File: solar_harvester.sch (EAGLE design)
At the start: 49 parts, among them U1 BQ25505, U2 TPS61322XA, U3 TPS61322XA, U4 MAX17040, U5 INA226

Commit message: schematic complete v01. Caps and diode selection needed
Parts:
- added B1: SOLAR_HARVESTER_M1_BOARD, vrlib_board:SOLAR_HARVESTER_M1_BOARD
- added C10, C9: 22u, vrlib_caps:1608_CAP
- added JP1: (no value), pinhead:PINHD-1X3
- added S1, S2: CONN_SCEW_TYPE_2P, vrlib_connector:CONN_SCEW_TYPE_2P
- added U$23, U$24, U$25, U$26, U$27: LOUT, vrlib_com_symbols:LOUT
- added U$28: GND, vrlib_com_symbols:GND
- C1: value 0.01uF -> 0.01u
- C2: value 4u7F -> 4u7
- C3: value 100uF -> 100u
- C4: value 4u7F -> 10u
- C5, C8: value 0.1uF -> 0.1u
- C6: value 1uF -> 1u
- C7: value 10nF -> 10n
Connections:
- new net GND1: C6.2, C7.2, C8.2, U4.CTG, U4.EO, U4.EP, U4.GND, U4.SEO, U5.A0, U5.A1, U5.GND
- net GND: now also C10.1, C9.1, S1.GND, S2.GND; no longer C6.2, C7.2, C8.2, U4.CTG, U4.EO, U4.EP, U4.GND, U4.SEO, U5.A0, U5.A1, U5.GND
- net I2C_SCL: now also JP1.3
- net I2C_SDA: now also JP1.2
- net VBAT_OK: now also JP1.1
- net VCC: no longer C4.1, C5.1
- net VDD3V3: now also C9.2, S1.VIN
- net VDD5: now also C10.2, S2.VIN
- net VIN_BAT: now also C4.1, C5.1, L2.1, L3.1
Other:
- note added: "I2C & BAT_OK PINHEAD"
- note added: "I2C ADDRESS 0110110"
- note added: "POWER"
- note added: "POWER BOOST"
- note added: "POWER HARVESTING"
- note added: "POWER MEASUREMENT"
- note added: "POWER OUTPUT"
- note added: "Universidad Jaime I. HPCA (High Performance Computer Architecture) Research Group"
- note added: "Vladislav Rykov"
- note added: "solar_harvester_m1"

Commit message: board routing started
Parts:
- removed BAT, SOLAR: CONN_SCEW_TYPE_2P, vrlib_connector:CONN_SCEW_TYPE_2P
- added BAT_IN, PV_IN: CONN_SCEW_TYPE_2P, vrlib_connector:CONN_SCEW_TYPE_2P
- added C11: 4u7, vrlib_caps:0603_CERAMIC
- added D1: JDH2S02SL, vrlib_diode:JDH2S02SL
- renumbered S1 to 3V3_OUT, S2 to 5V_OUT
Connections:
- removed net VCC: C8.1, U1.VOC_SAMP, U1.VSTOR, U5.VS
- new net N$9: D1.P$2, PV_IN.VIN
- new net VSTOR: C11.1, C5.1, C8.1, U1.VOC_SAMP, U1.VSTOR, U5.VS
- net GND: now also BAT_IN.GND, C11.2, PV_IN.GND; no longer BAT.GND, SOLAR.GND
- net PVIN: now also D1.P$1; no longer SOLAR.VIN
- net VIN_BAT: now also BAT_IN.VIN; no longer BAT.VIN, C5.1
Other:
- moved on the sheet: C4, C5

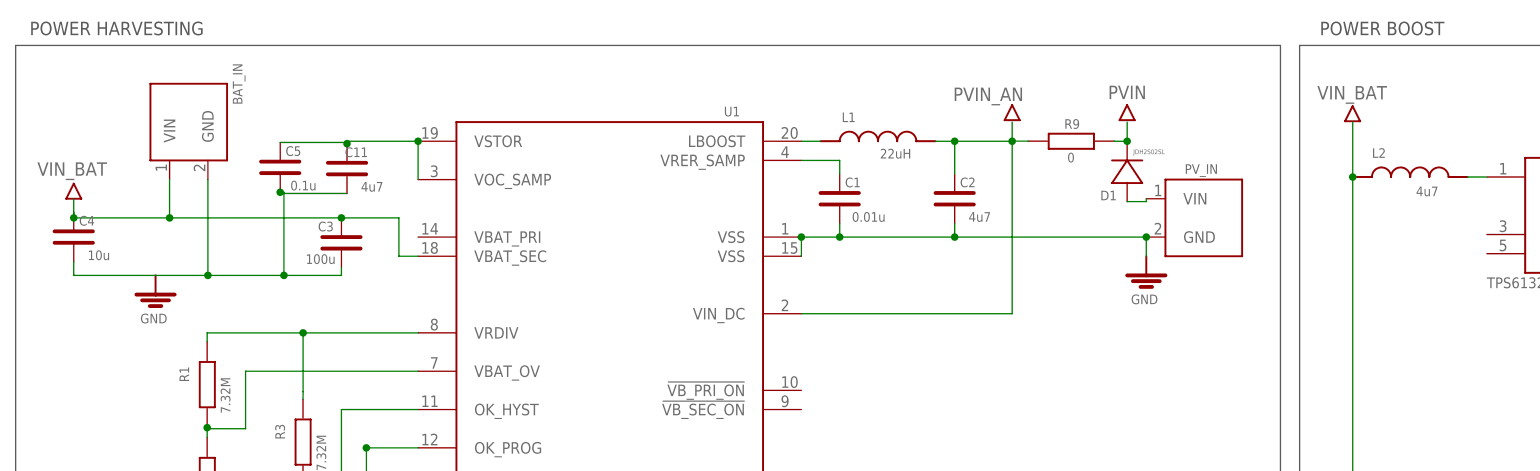
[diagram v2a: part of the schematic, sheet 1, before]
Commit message: bq25505, both tps622, max17004 routed
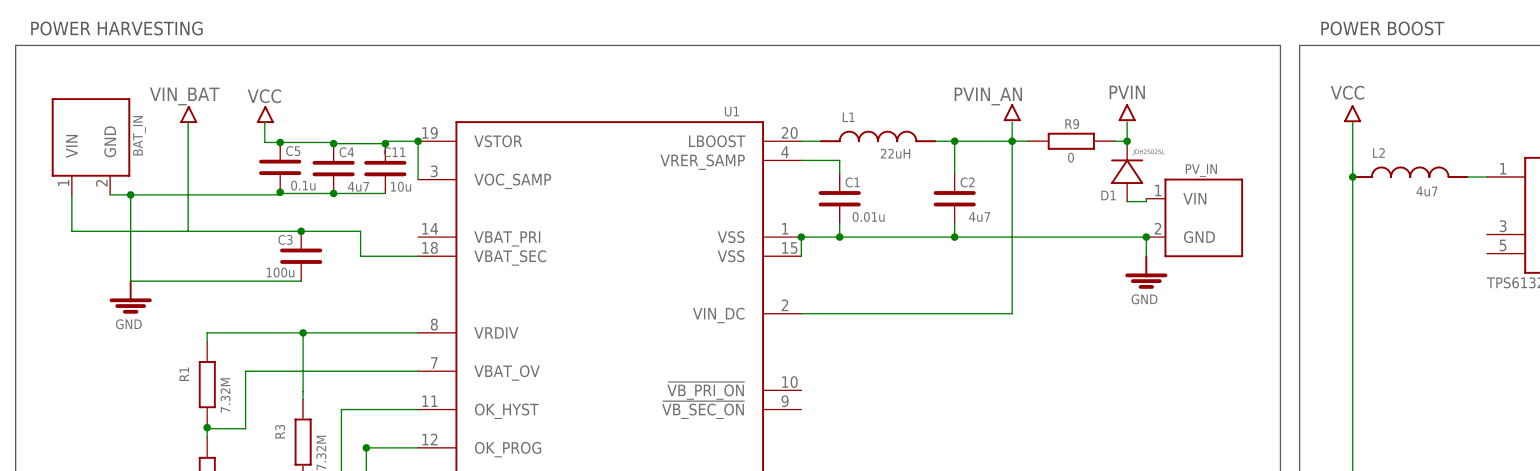
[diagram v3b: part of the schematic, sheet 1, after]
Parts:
- added U$29: LOUT, vrlib_com_symbols:LOUT
- C11: value 4u7 -> 10u
- C4: value 10u -> 4u7
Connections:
- removed net GND1: C6.2, C7.2, C8.2, U4.CTG, U4.EO, U4.EP, U4.GND, U4.SEO, U5.A0, U5.A1, U5.GND
- removed net VSTOR: C11.1, C5.1, C8.1, U1.VOC_SAMP, U1.VSTOR, U5.VS
- new net VCC: C11.1, C4.1, C5.1, C8.1, L2.1, L3.1, U1.VOC_SAMP, U1.VSTOR, U5.VS
- net GND: now also C6.2, C7.2, C8.2, U4.CTG, U4.EO, U4.EP, U4.GND, U4.SEO, U5.A0, U5.A1, U5.GND
- net VIN_BAT: no longer C4.1, L2.1, L3.1
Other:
- moved on the sheet: BAT_IN, C11, C3, C4

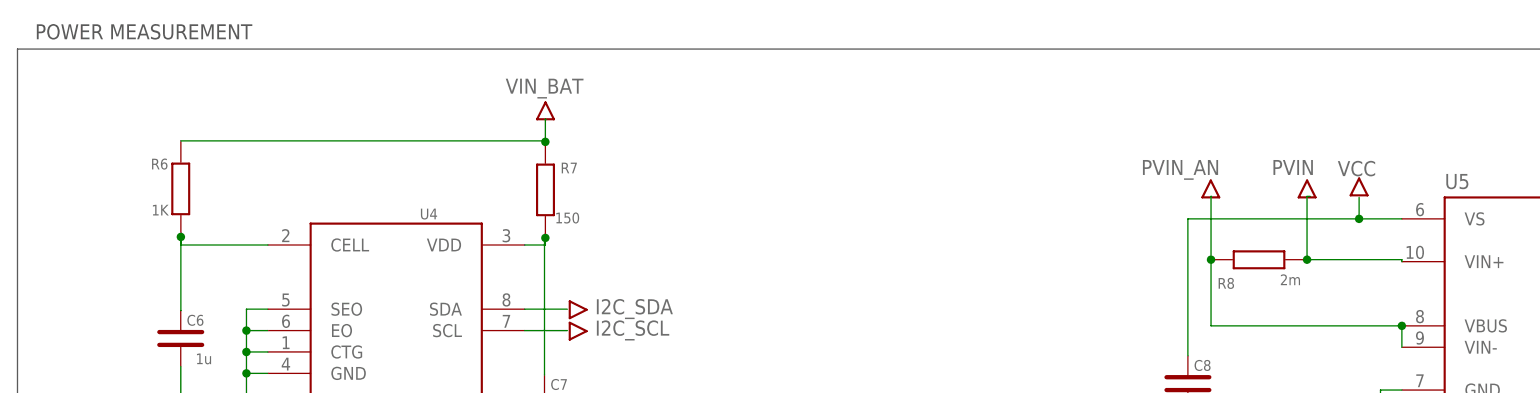
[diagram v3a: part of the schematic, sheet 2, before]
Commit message: routing complete without battery under-voltage protection
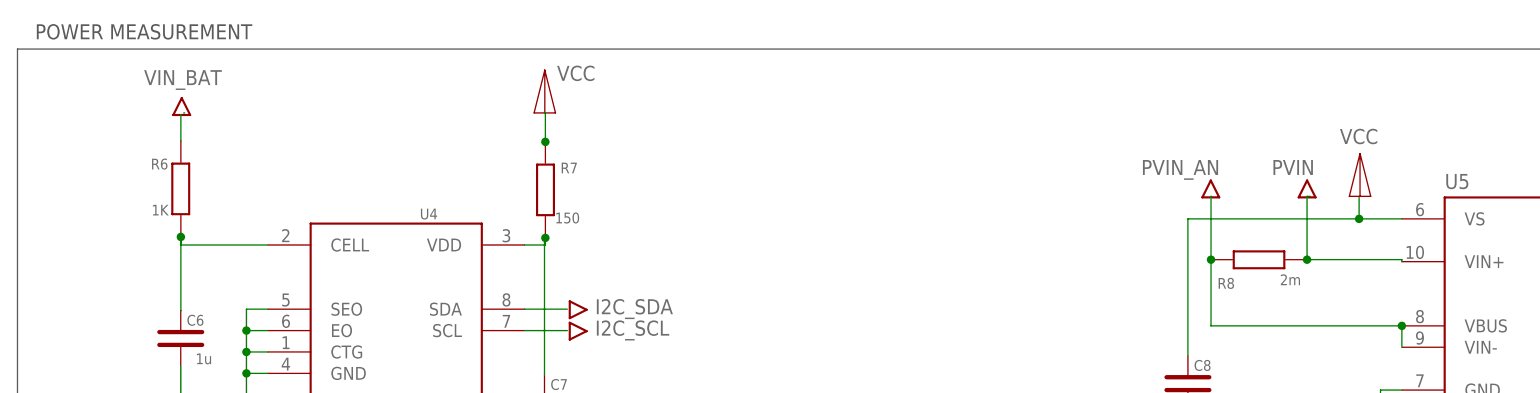
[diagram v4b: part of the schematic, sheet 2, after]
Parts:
- removed U$1, U$11, U$13, U$14, U$15, U$16, U$17, U$18, U$2, U$21, U$22, U$23, U$24, U$25, U$26, U$27, U$29, U$3, U$5, U$7, U$9: LOUT, vrlib_com_symbols:LOUT
- removed U$10, U$12, U$19, U$20, U$28, U$4, U$6, U$8: GND, vrlib_com_symbols:GND
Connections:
- net VCC: now also R7.P$2
- net VIN_BAT: no longer R7.P$2
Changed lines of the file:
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@@
 <part name="U$10" library="vrlib_com_symbols" deviceset="GND" device=""/>
 <part name="C5" library="vrlib_caps" deviceset="0603_CERAMIC" device="" value="0.1u"/>
-<part name="U$11" library="vrlib_com_symbols" deviceset="LOUT" device=""/>
+<part name="U$11" library="vrlib_com_symbols" deviceset="VCC" device=""/>
 <part name="R1" library="vrlib_res" deviceset="RESISITOR_0603" device="" value="7.32M"/>
 <part name="R2" library="vrlib_res" deviceset="RESISITOR_0603" device="" value="5.62M"/>
@@
 <part name="C7" library="vrlib_caps" deviceset="0603_CERAMIC" device="" value="10n"/>
 <part name="U$4" library="vrlib_com_symbols" deviceset="GND" device=""/>
-<part name="U$5" library="vrlib_com_symbols" deviceset="LOUT" device=""/>
 <part name="U$12" library="vrlib_com_symbols" deviceset="GND" device=""/>
 <part name="R8" library="vrlib_res" deviceset="RESISITOR_0603" device="" value="2m"/>
@@
 <part name="C9" library="vrlib_caps" deviceset="1608_CAP" device="" value="22u"/>
 <part name="C10" library="vrlib_caps" deviceset="1608_CAP" device="" value="22u"/>
-<part name="U$23" library="vrlib_com_symbols" deviceset="LOUT" device=""/>
 <part name="B1" library="vrlib_board" deviceset="SOLAR_HARVESTER_M1_BOARD" device=""/>
 <part name="JP1" library="pinhead" library_urn="urn:adsk.eagle:library:325" deviceset="PINHD-1X3" device="" package3d_urn="urn:adsk.eagle:package:22458/2"/>
@@
 <part name="U$29" library="vrlib_com_symbols" deviceset="LOUT" device=""/>
 <part name="C4" library="vrlib_caps" deviceset="0603_CERAMIC" device="" value="4u7"/>
+<part name="U$31" library="vrlib_com_symbols" deviceset="VCC" device=""/>
+<part name="U$23" library="vrlib_com_symbols" deviceset="VCC" device=""/>
+<part name="U$30" library="vrlib_com_symbols" deviceset="VCC" device=""/>
 </parts>
 <sheets>
@@
 <attribute name="VALUE" x="234.37" y="138.008" size="1.27" layer="96"/>
 </instance>
-<instance part="U$23" gate="G$1" x="187.364" y="157.592" smashed="yes"/>
 <instance part="B1" gate="G$1" x="32" y="15" smashed="yes">
 <attribute name="NAME" x="29.46" y="20.08" size="1.778" layer="95" font="vector"/>
@@
 <attribute name="VALUE" x="57.128" y="149.542" size="1.27" layer="96" rot="R180"/>
 </instance>
+<instance part="U$31" gate="G$1" x="187.278" y="157.48" smashed="yes"/>
 </instances>
 <busses>
@@
 <wire x1="45.224" y1="154.78" x2="43.18" y2="154.78" width="0.1524" layer="91"/>
 <wire x1="43.18" y1="154.78" x2="43.18" y2="157.48" width="0.1524" layer="91"/>
-<label x="40.894" y="160.02" size="1.778" layer="95"/>
+<label x="40.894" y="163.068" size="1.778" layer="95"/>
 <pinref part="C4" gate="G$1" pin="1"/>
 <wire x1="45.224" y1="154.78" x2="52.302" y2="154.78" width="0.1524" layer="91"/>
@@
 <wire x1="187.38" y1="150.2" x2="187.38" y2="157.48" width="0.1524" layer="91"/>
 <junction x="187.38" y="150.2"/>
-<label x="184.458" y="160.48" size="1.778" layer="95"/>
+<label x="184.712" y="163.02" size="1.778" layer="95"/>
 </segment>
 </net>
@@
 <attribute name="VALUE" x="182.34" y="121.28" size="1.778" layer="96"/>
 </instance>
-<instance part="U$1" gate="G$1" x="75.6" y="158.504" smashed="yes"/>
+<instance part="U$1" gate="G$1" x="32.42" y="159.012" smashed="yes"/>
 <instance part="R6" gate="G$1" x="32.3" y="150.238" smashed="yes" rot="R270">
 <attribute name="NAME" x="28.74" y="152.552" size="1.27" layer="95"/>
@@
 </instance>
 <instance part="U$4" gate="G$1" x="58" y="112.92" smashed="yes"/>
-<instance part="U$5" gate="G$1" x="172.18" y="149.474" smashed="yes"/>
 <instance part="U$12" gate="G$1" x="192.96" y="118.66" smashed="yes"/>
 <instance part="R8" gate="G$1" x="160.302" y="141.82" smashed="yes">
@@
 </instance>
 <instance part="U$22" gate="G$1" x="154.578" y="149.234" smashed="yes"/>
+<instance part="U$23" gate="G$1" x="75.518" y="159.258" smashed="yes"/>
+<instance part="U$30" gate="G$1" x="172.292" y="149.352" smashed="yes"/>
 </instances>
 <busses>
@@
 <segment>
 <pinref part="R6" gate="G$1" pin="P$1"/>
-<pinref part="R7" gate="G$1" pin="P$2"/>
-<wire x1="32.316" y1="155.938" x2="75.584" y2="155.938" width="0.1524" layer="91"/>
-<wire x1="75.584" y1="155.938" x2="75.584" y2="155.822" width="0.1524" layer="91"/>
-<label x="70.866" y="161.544" size="1.778" layer="95"/>
-<wire x1="75.584" y1="155.822" x2="75.584" y2="158.496" width="0.1524" layer="91"/>
-<wire x1="75.584" y1="158.496" x2="75.692" y2="158.496" width="0.1524" layer="91"/>
-<junction x="75.584" y="155.822"/>
+<wire x1="32.316" y1="155.938" x2="32.316" y2="159.004" width="0.1524" layer="91"/>
+<wire x1="32.316" y1="159.004" x2="32.258" y2="159.004" width="0.1524" layer="91"/>
+<label x="27.94" y="162.56" size="1.778" layer="95"/>
 </segment>
 </net>
@@
 <wire x1="177.26" y1="146.68" x2="172.18" y2="146.68" width="0.1524" layer="91"/>
 <wire x1="172.18" y1="146.68" x2="172.18" y2="149.22" width="0.1524" layer="91"/>
-<label x="169.64" y="151.76" size="1.778" layer="95"/>
+<label x="169.894" y="155.57" size="1.778" layer="95"/>
 <pinref part="C8" gate="G$1" pin="1"/>
 <wire x1="151.86" y1="130.424" x2="151.86" y2="146.68" width="0.1524" layer="91"/>
 <wire x1="151.86" y1="146.68" x2="172.18" y2="146.68" width="0.1524" layer="91"/>
 <junction x="172.18" y="146.68"/>
+</segment>
+<segment>
+<pinref part="R7" gate="G$1" pin="P$2"/>
+<wire x1="75.584" y1="155.938" x2="75.584" y2="155.822" width="0.1524" layer="91"/>
+<wire x1="75.584" y1="155.822" x2="75.584" y2="159.258" width="0.1524" layer="91"/>
+<wire x1="75.584" y1="159.258" x2="75.438" y2="159.258" width="0.1524" layer="91"/>
+<junction x="75.584" y="155.822"/>
+<label x="76.962" y="163.068" size="1.778" layer="95"/>
 </segment>
 </net>
@@
 </segment>
 </net>
+<net name="N$12" class="0">
+<segment>
+<wire x1="32.658" y1="159.258" x2="32.766" y2="159.258" width="0.1524" layer="91"/>
+</segment>
+</net>

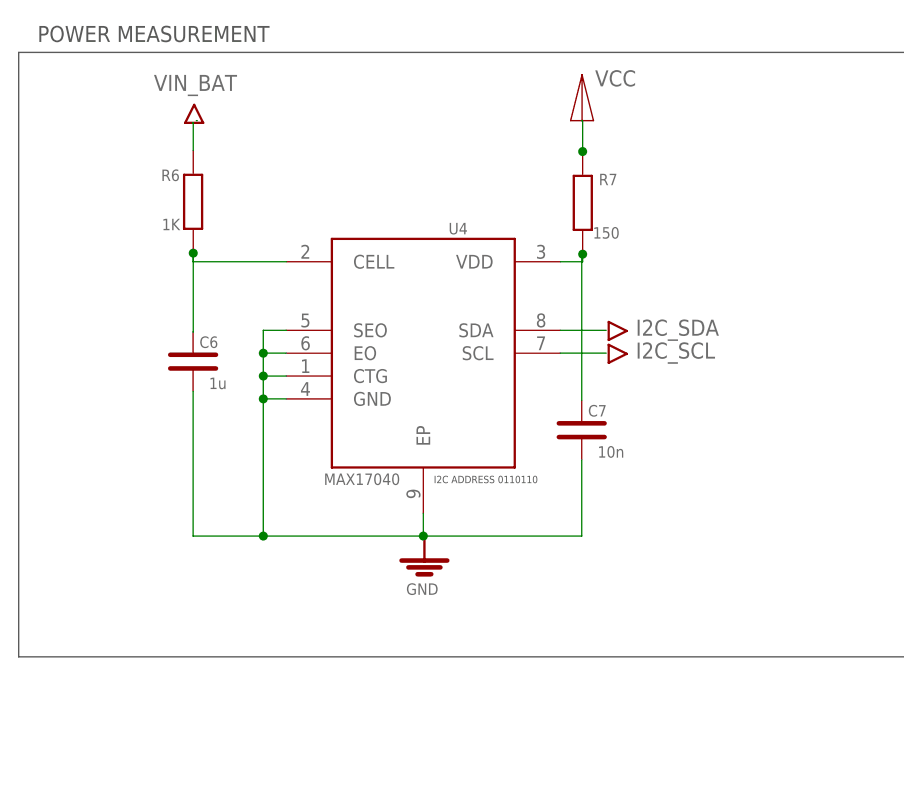
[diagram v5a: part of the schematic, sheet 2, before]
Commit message: Routing done, without uv protection
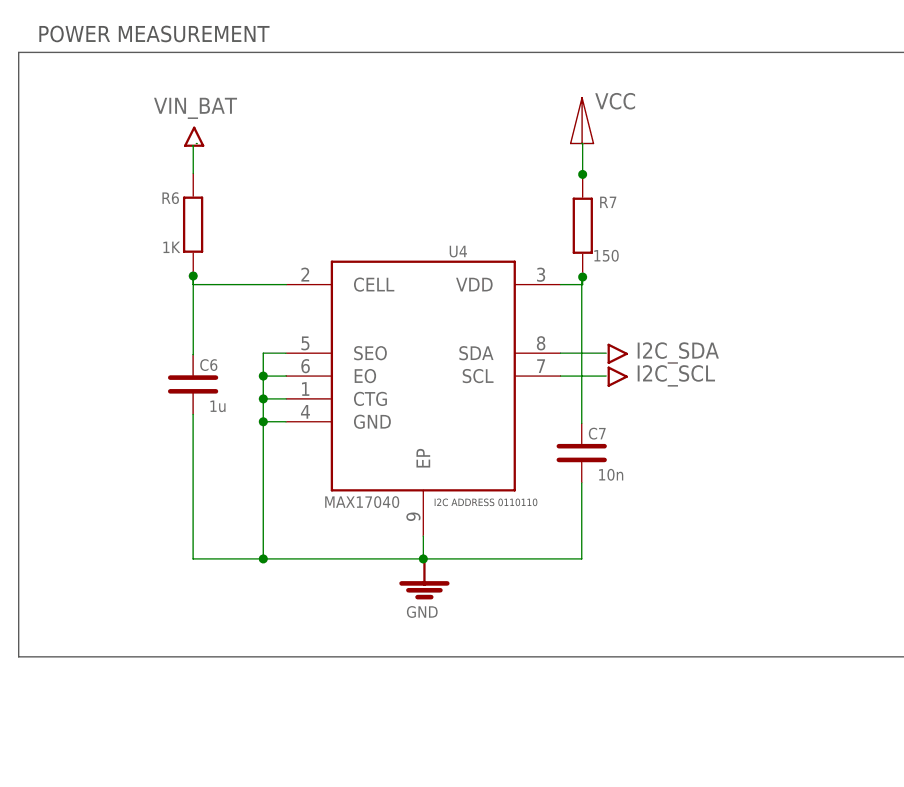
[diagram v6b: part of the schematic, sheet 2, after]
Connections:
- net I2C_SCL: now also JP1.1; no longer JP1.3
- net VBAT_OK: now also JP1.3; no longer JP1.1
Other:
- moved on the sheet: C6, C7, R6, R7, U4
